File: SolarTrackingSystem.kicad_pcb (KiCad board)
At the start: 2 copper layers, 57 x 54 mm, 8 parts, among them J1 Servo Pin Connector, J2 LDR Terminal, J3 LDR Terminal (1)

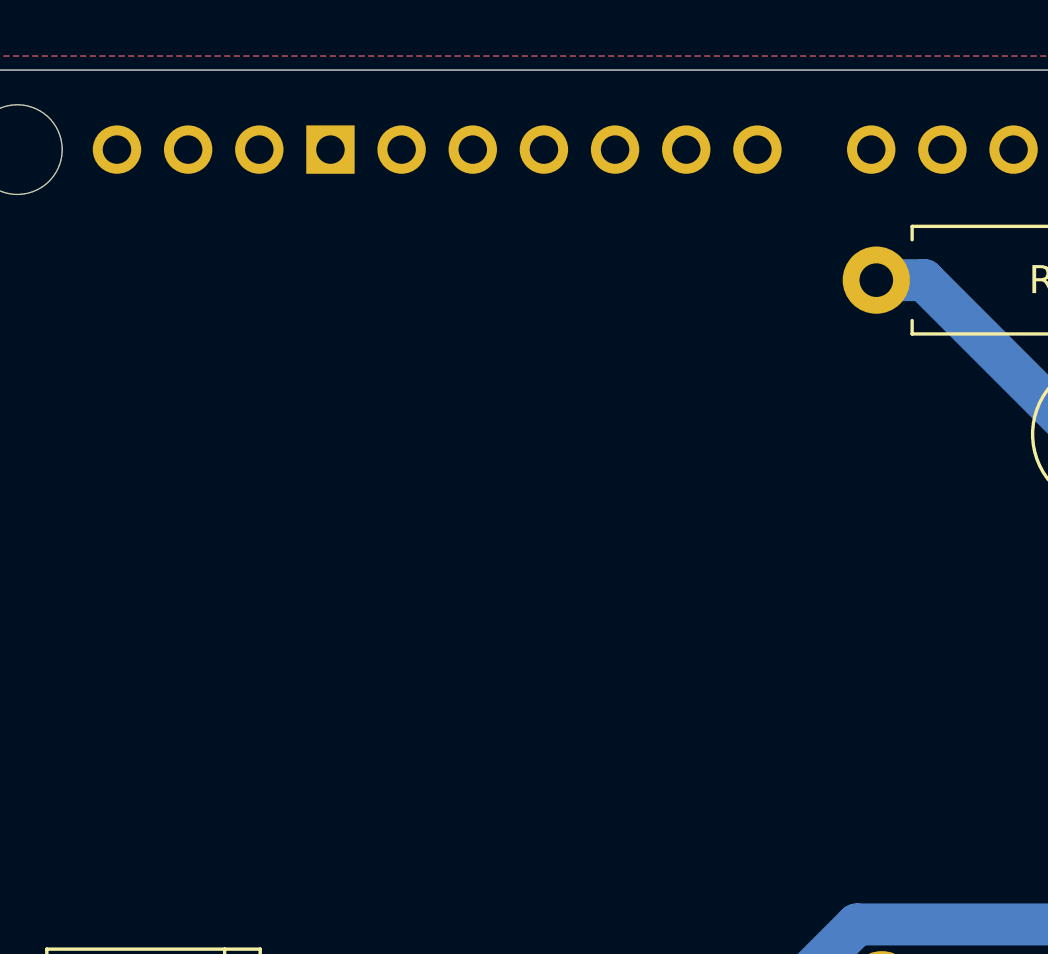
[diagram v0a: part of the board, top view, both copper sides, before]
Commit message: added LED Debug Indicator
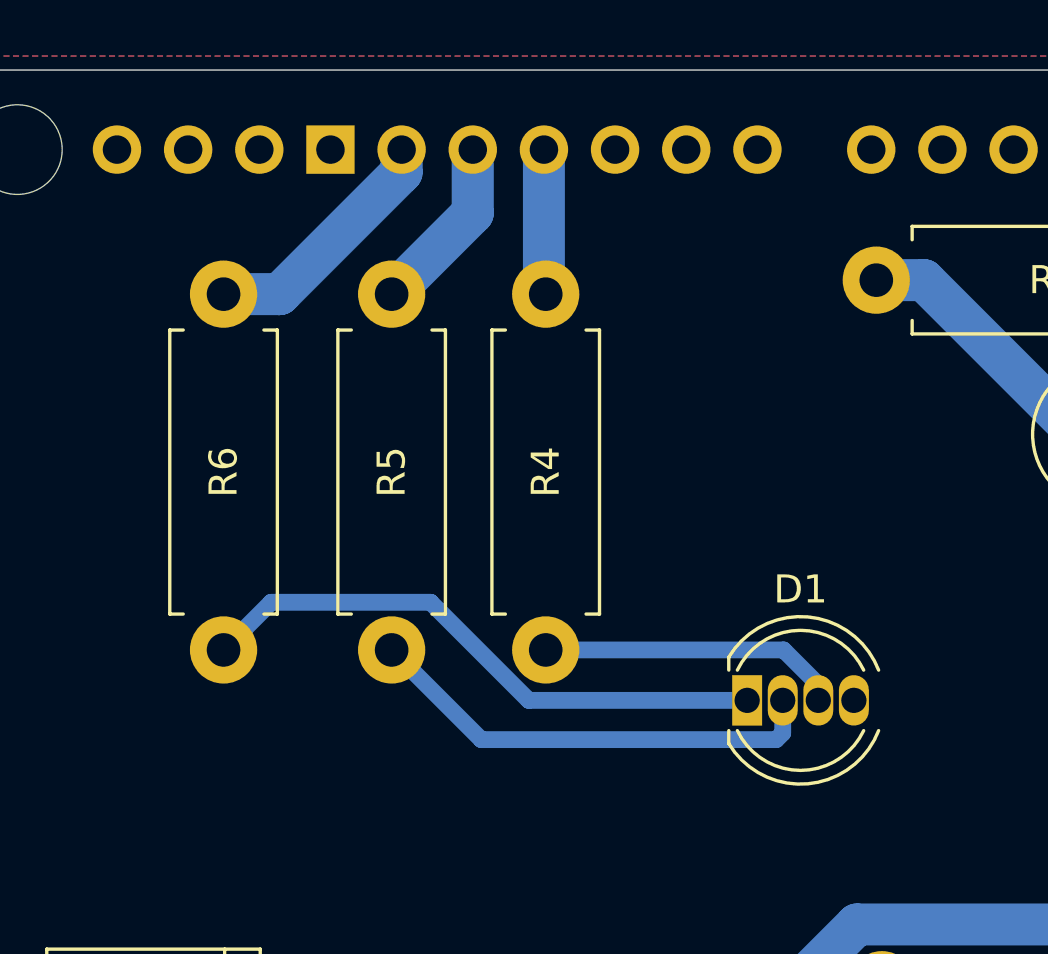
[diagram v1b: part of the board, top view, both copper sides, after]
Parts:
- added D1: LED Debugging Indicator, LED_THT:LED_D5.0mm-4_RGB, F.Cu at (140.2, 81.0)
- added R4: 1k, Resistor_THT:R_Axial_DIN0411_L9.9mm_D3.6mm_P12.70mm_Horizontal, F.Cu at (133.0, 66.5)
- added R5: 1k, Resistor_THT:R_Axial_DIN0411_L9.9mm_D3.6mm_P12.70mm_Horizontal, F.Cu at (127.5, 66.5)
- added R6: 1k, Resistor_THT:R_Axial_DIN0411_L9.9mm_D3.6mm_P12.70mm_Horizontal, F.Cu at (121.5, 66.5)
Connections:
- A1 pad D11: unconnected-(A1-PadD11) -> Net-(A1-PadD11)
- A1 pad D12: unconnected-(A1-PadD12) -> Net-(A1-PadD12)
- A1 pad D13: unconnected-(A1-PadD13) -> Net-(A1-PadD13)
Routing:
- net Net-(D1-BA): track 0.00 -> 20.8 mm
- net Net-(D1-GA): track 0.00 -> 16.5 mm
- net Net-(D1-RA): track 0.00 -> 10.8 mm
- net Net-(A1-PadD13): track 0.00 -> 8.96 mm
- net Net-(A1-PadD12): track 0.00 -> 6.36 mm
- net Net-(A1-PadD11): track 0.00 -> 5.19 mm

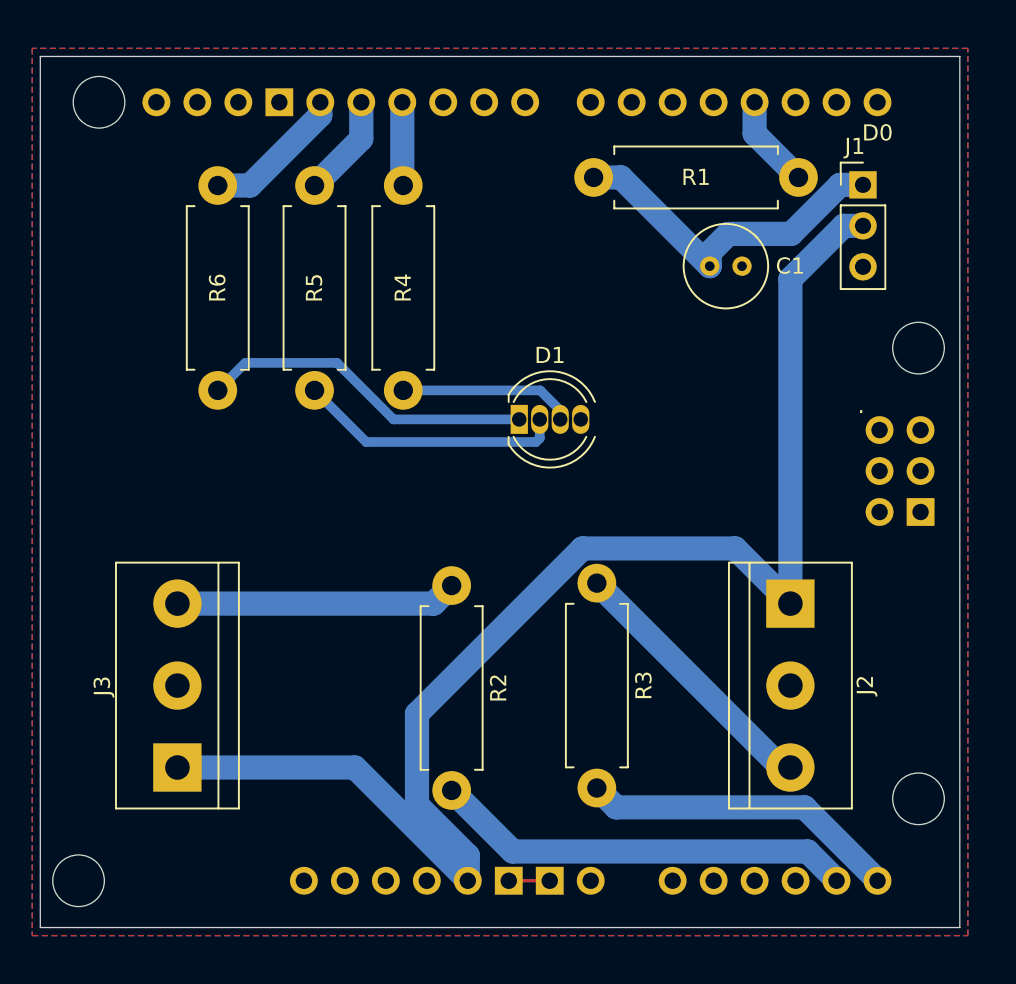
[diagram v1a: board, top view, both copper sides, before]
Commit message: new feature
added real-time clock
changed from single sided pcb to double sided
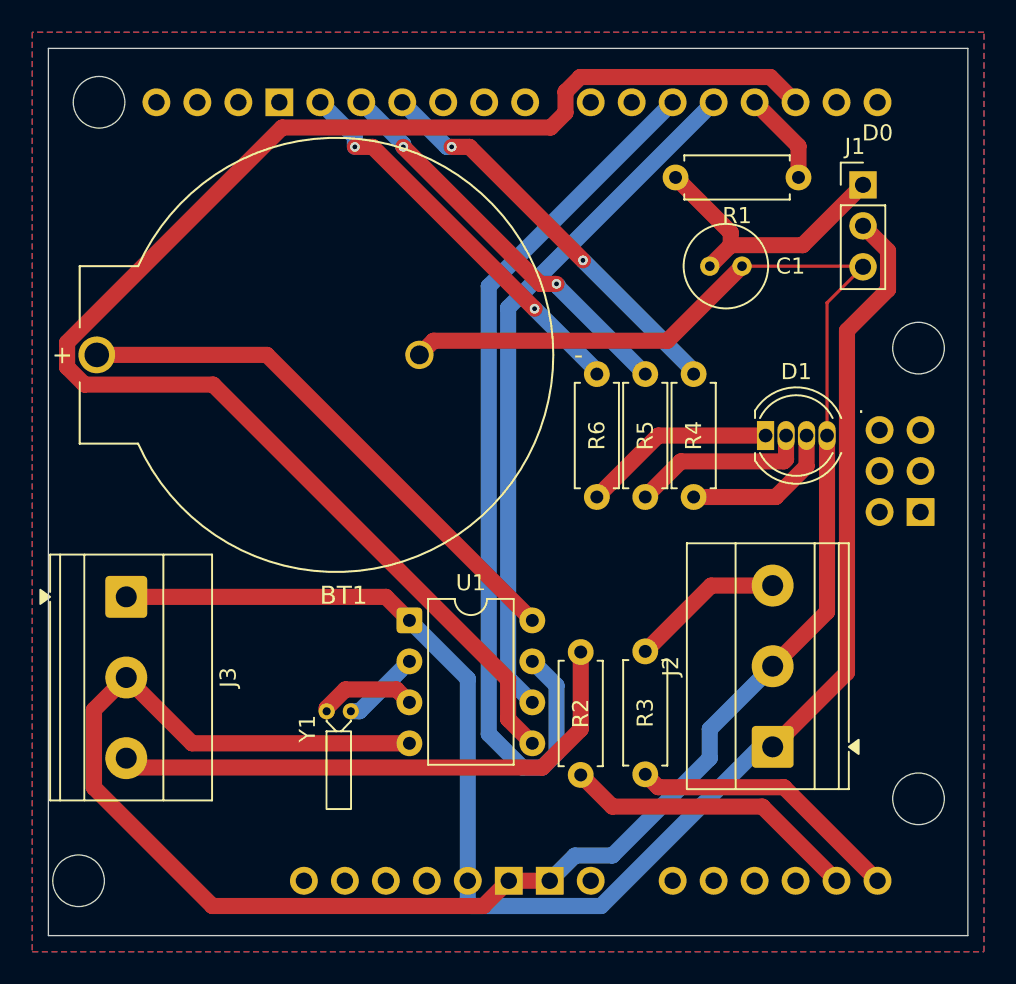
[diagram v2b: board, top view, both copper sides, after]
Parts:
- added BT1: BS-2450, BS-2450:BAT_BS-2450, F.Cu at (128.9, 77.0)
- added U1: DS1302+, Package_DIP:DIP-8_W7.62mm, F.Cu at (133.4, 93.5)
- added Y1: Crystal, Crystal:Crystal_DS10_D1.0mm_L4.3mm_Horizontal, F.Cu at (128.2, 99.1)
- J2, J3: footprint TerminalBlock:TerminalBlock_bornier-3_P5.08mm -> TerminalBlock_Phoenix:TerminalBlock_Phoenix_MKDS-1,5-3_1x03_P5.00mm_Horizontal
- R1, R2, R3, R4, R5, R6: footprint Resistor_THT:R_Axial_DIN0411_L9.9mm_D3.6mm_P12.70mm_Horizontal -> Resistor_THT:R_Axial_DIN0207_L6.3mm_D2.5mm_P7.62mm_Horizontal
- moved R6 26.2 mm to (145.0, 78.2)
- moved R5 23.6 mm to (148.0, 78.2)
- moved R4 21.5 mm to (151.0, 78.2)
- moved D1 15.3 mm to (155.5, 82.0)
- moved J3 11.0 mm to (115.8, 92.0), turned to -90 degrees
- moved R2 9.00 mm to (144.0, 95.4)
- moved J2 8.95 mm to (155.9, 101.3), turned to 90 degrees
- moved R3 5.19 mm to (148.0, 95.4)
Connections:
- A1 pad D2: unconnected-(A1-D2_INT0-PadD2) -> /RTC_RST
- A1 pad D4: unconnected-(A1-PadD4) -> /RTC_DATA
- A1 pad D5: unconnected-(A1-PadD5) -> /RTC_CLK
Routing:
- net GND: track 2.60 -> 136.2 mm
- net /RTC_RST: track 0.00 -> 94.8 mm
- net /RTC_CLK: track 0.00 -> 55.6 mm
- net /RTC_DATA: track 0.00 -> 43.1 mm
- net Net-(U1-VCC1): track 0.00 -> 33.8 mm
- net Net-(A1-PadD11): track 5.19 -> 25.2 mm, vias 0 -> 2
- net Net-(A1-PadD12): track 6.36 -> 24.8 mm, vias 0 -> 2
- net Net-(J3-Pin_3): track 17.5 -> 34.2 mm
- net Net-(A1-PadD13): track 8.96 -> 24.6 mm, vias 0 -> 2
- net Net-(D1-BA): track 20.8 -> 12.0 mm
- net /5V_pin: track 87.4 -> 96.2 mm
- net Net-(A1-PadA4): track 26.2 -> 18.6 mm
- net Net-(J2-Pin_3): track 16.7 -> 9.59 mm
- net Net-(U1-X2): track 0.00 -> 6.14 mm
- net Net-(D1-GA): track 16.5 -> 11.2 mm
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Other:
- board size 57 x 54 mm -> 57 x 55 mm
